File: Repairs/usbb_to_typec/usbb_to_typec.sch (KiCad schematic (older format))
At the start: 5 parts, among them J1 USB_B, J2 USB_C_Receptacle_USB2.0

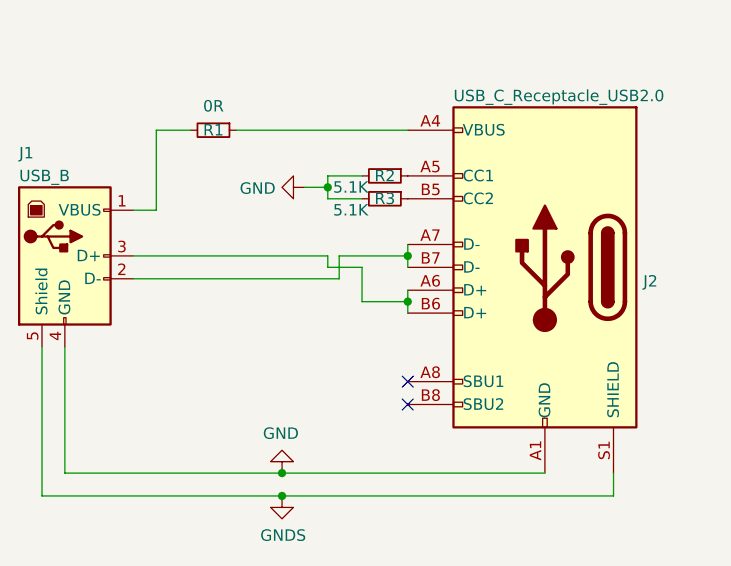
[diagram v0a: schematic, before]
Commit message: Gerber export setting fixes - mostly changing "(excludeedgelayer false)" to "true)"
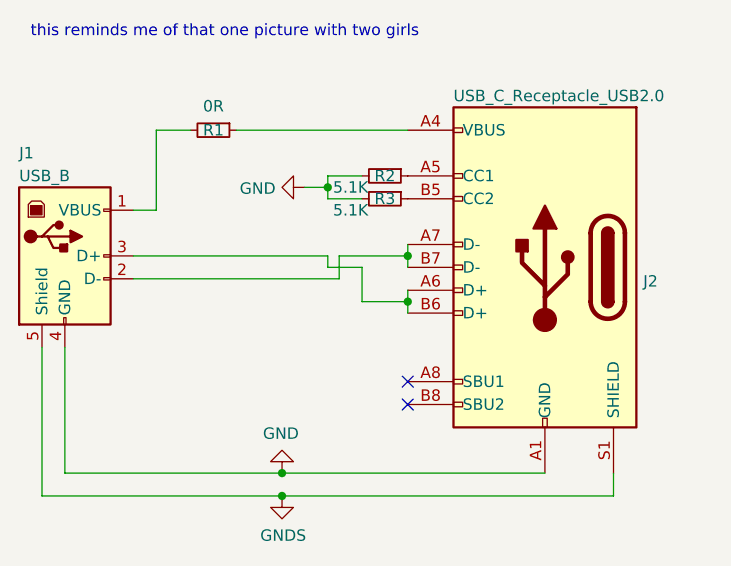
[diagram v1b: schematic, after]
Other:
- note added: "this reminds me of that one picture with two girls"
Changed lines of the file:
@@
 	-1   0    0    -1
 $EndComp
+Text Notes 4950 2850 0    50   ~ 0
+this reminds me of that one picture with two girls
 $EndSCHEMATC
